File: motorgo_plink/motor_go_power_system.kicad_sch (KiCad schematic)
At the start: 22 parts, among them U6 TPS54620RHLR, U8 AMS1117-3.3

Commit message: production files and all edits for final send off of v1.0
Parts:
- C1: value 30pF 0Ohm -> 68pf
- C15, C19, C2: value 10uF 1mOhm -> 4.7uF 1mOhm
- C20: value 16nF 0Ohm -> 6.8nf
- L1: value 3.3uH 14.3mOhm -> 2.2uH 12.7mOhm; LCSC_Part_Number C5370922 -> C5440776
- R19: value 4.02k -> 3.92k
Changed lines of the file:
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@@
 			)
 		)
-		(property "Value" "10uF 1mOhm"
+		(property "Value" "4.7uF 1mOhm"
 			(at 32.004 78.486 0)
 			(effects
@@
 			)
 		)
-		(property "Value" "4.02k"
+		(property "Value" "3.92k"
 			(at 81.28 98.425 0)
 			(effects
@@
 			)
 		)
-		(property "Value" "16nF 0Ohm"
+		(property "Value" "6.8nf"
 			(at 75.057 108.839 0)
 			(effects
@@
 			)
 		)
-		(property "Value" "10uF 1mOhm"
+		(property "Value" "4.7uF 1mOhm"
 			(at 32.004 80.518 0)
 			(effects
@@
 			)
 		)
-		(property "Value" "30pF 0Ohm"
+		(property "Value" "68pf"
 			(at 90.805 106.68 0)
 			(effects
@@
 			)
 		)
-		(property "Value" "3.3uH 14.3mOhm"
+		(property "Value" "2.2uH 12.7mOhm"
 			(at 135.255 63.5 90)
 			(effects
@@
 			)
 		)
-		(property "LCSC_Part_Number" "C5370922"
+		(property "LCSC_Part_Number" "C5440776"
 			(at 134.62 65.405 0)
 			(effects
@@
 			)
 		)
-		(property "Value" "10uF 1mOhm"
+		(property "Value" "4.7uF 1mOhm"
 			(at 32.004 76.454 0)
 			(effects

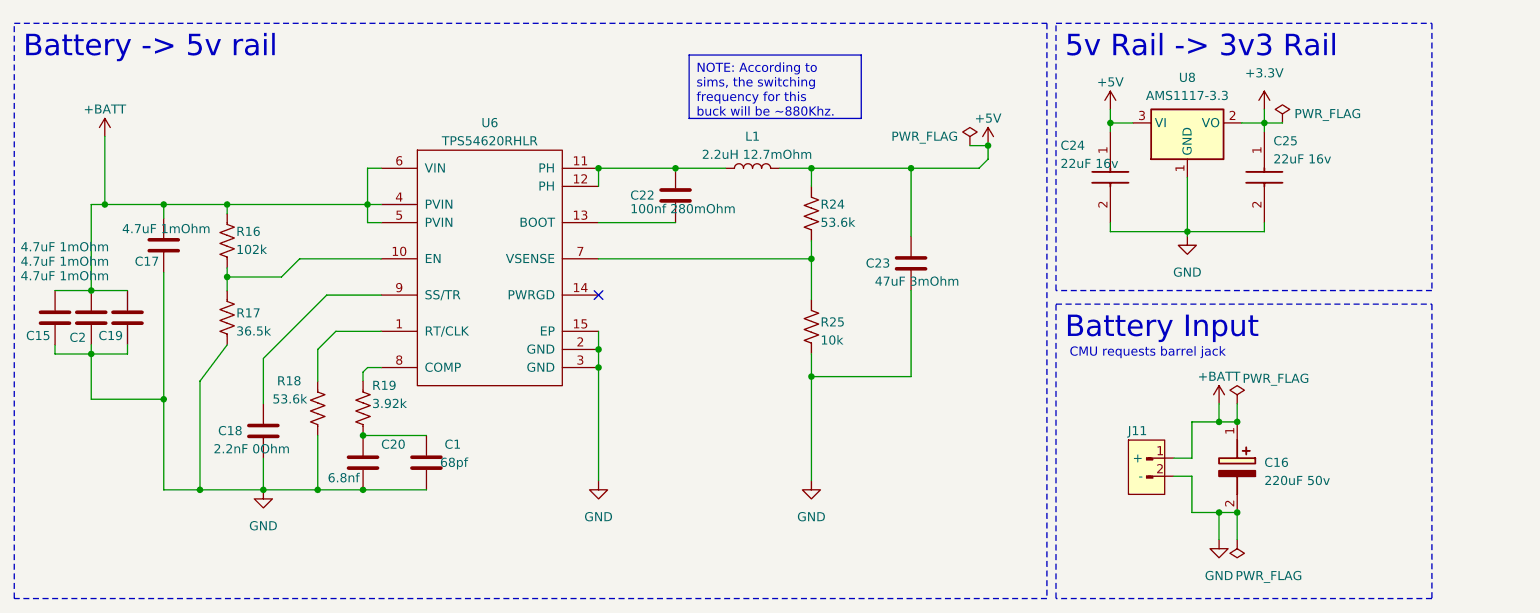
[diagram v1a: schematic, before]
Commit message: updated schematic to fix IMU i2c mismatch, silkscreen readability, schottky backpower diode, and added RC Servo pins
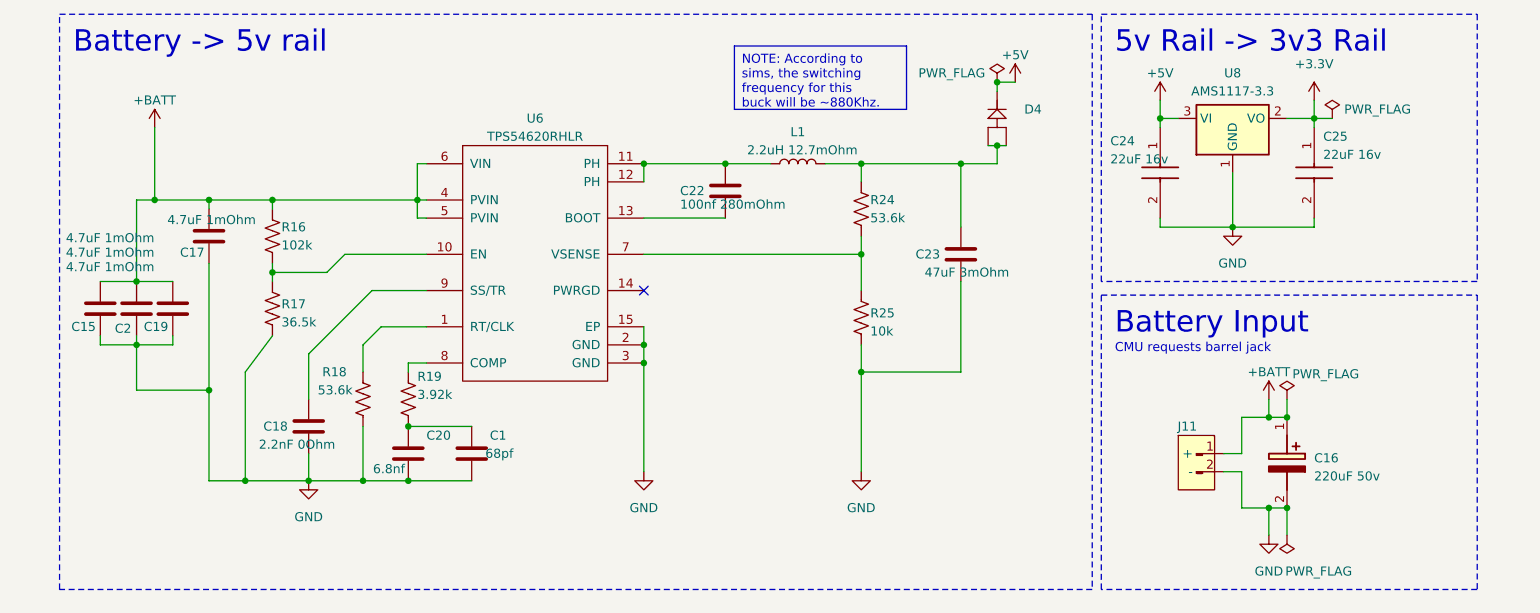
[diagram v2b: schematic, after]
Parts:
- added D4: Schottky_SB1045L_C908747, easyeda:TO-277_3P-L5.4-W4.0-LS6.5-TR, symbol easyeda:Schottky_SB1045L_C908747
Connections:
- net +5V: now also D4.2 (K); no longer C23.1, L1.2, R24.1
- new net: C23.1, D4.1 (A), D4.3 (A), L1.2, R24.1
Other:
- moved on the sheet: C1, C15, C16, C17, C18, C19, C2, C20, C22, C23, C24, C25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

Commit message: update to recent production files
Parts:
- C1, C18, C20: footprint Capacitor_SMD:C_0201_0603Metric -> Capacitor_SMD:C_0402_1005Metric
- D4: value Schottky_SB1045L_C908747 -> Schottky_SB1045L_C908747 10A; LCSC_Part_Number (none) -> C908747
- L1: value 2.2uH 12.7mOhm -> 2.2uH 12.7mOhm C5440776
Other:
- note added: "10A 10v"
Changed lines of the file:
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@@
+		)
+	)
+	(text "10A\n10v"
+		(exclude_from_sim no)
+		(at 173.228 61.214 0)
+		(effects
+			(font
+				(size 1.27 1.27)
+			)
 		)
 	)
@@
 			)
 		)
-		(property "Footprint" "Capacitor_SMD:C_0201_0603Metric"
+		(property "Footprint" "Capacitor_SMD:C_0402_1005Metric"
 			(at 87.3252 109.22 0)
 			(effects
@@
 		(on_board yes)
 		(dnp no)
-		(fields_autoplaced yes)
 		(property "Reference" "D4"
-			(at 172.72 57.1499 90)
-			(effects
-				(font
-					(size 1.27 1.27)
-				)
-				(justify left)
-			)
-		)
-		(property "Value" "Schottky_SB1045L_C908747"
+			(at 171.958 57.15 90)
+			(effects
+				(font
+					(size 1.27 1.27)
+				)
+				(justify left)
+			)
+		)
+		(property "Value" "Schottky_SB1045L_C908747 10A"
 			(at 172.72 59.6899 90)
 			(effects
@@
 			)
 		)
-		(property "Description" ""
+		(property "Description" "High amps for whole 5V rail"
 			(at 168.91 58.42 0)
 			(effects
@@
 		(property "uuid" "std:209a628ebac24c2f8df90420eba7d942"
 			(at 159.004 58.42 0)
+			(effects
+				(font
+					(size 1.27 1.27)
+				)
+				(hide yes)
+			)
+		)
+		(property "LCSC_Part_Number" "C908747"
+			(at 168.91 58.42 0)
 			(effects
 				(font
@@
 			)
 		)
-		(property "Footprint" "Capacitor_SMD:C_0201_0603Metric"
+		(property "Footprint" "Capacitor_SMD:C_0402_1005Metric"
 			(at 96.2152 109.22 0)
 			(effects
@@
 			)
 		)
-		(property "Value" "2.2uH 12.7mOhm"
+		(property "Value" "2.2uH 12.7mOhm C5440776"
 			(at 141.605 62.865 90)
 			(effects
@@
 			)
 		)
-		(property "Footprint" "Capacitor_SMD:C_0201_0603Metric"
+		(property "Footprint" "Capacitor_SMD:C_0402_1005Metric"
 			(at 73.3552 105.41 0)
 			(effects
